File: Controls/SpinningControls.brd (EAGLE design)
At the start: 209.6 x 107.9 mm, 120 parts, among them IC1 S-19246E33H-V5T2U, IC2 SN74LVC1G34DBVR, IC3 SN74LVC1G34DBVR, IC4 SN74LVC1G34DBVR, IC5 TXS0104EDR, J10 SULLINS_PPPC062LFBN-RCSULLINS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, J11 SULLINS_PPPC062LFBN-RCSULLINS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, J12 SULLINS_PPPC062LFBN-RCSULLINS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, J13 SULLINS_PPPC062LFBN-RCSULLINS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, J14 SULLINS_PPPC062LFBN-RCSULLINS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

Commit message: dan tings, 50ohm FPGA inline, 3v3 to 5 logic for SR
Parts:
- R20: device rcl:R0603 -> rcl:R0402
- R5: value (none) -> 10k; device rcl:R0402 -> rcl:R0603
- moved R56 206.3 mm to (113.5, 45.2)
- moved R55 204.4 mm to (112.3, 47.6), turned to 45 degrees
- moved R54 199.1 mm to (108.3, 47.6), turned to 45 degrees
- moved R53 193.6 mm to (104.2, 47.6), turned to 90 degrees
- moved R52 188.7 mm to (101.1, 47.6), turned to 90 degrees
- moved R51 183.8 mm to (98.0, 47.6), turned to 90 degrees
- moved R50 178.9 mm to (94.9, 47.6), turned to 90 degrees
- moved R49 173.5 mm to (90.8, 47.6), turned to 90 degrees
- moved R48 168.6 mm to (87.8, 47.6), turned to 90 degrees
- moved R47 163.9 mm to (84.9, 47.6), turned to 90 degrees
- moved R46 159.1 mm to (82.0, 47.6), turned to 90 degrees
- moved R45 154.0 mm to (78.5, 47.6), turned to 135 degrees
- moved R38 153.2 mm to (113.5, 42.7)
- moved R44 147.8 mm to (73.0, 47.5), turned to 180 degrees
- moved R35 145.8 mm to (102.6, 47.6), turned to 270 degrees
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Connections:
- net 3V3_LOGIC: now also R5.2; no longer R20.2
- net ENC_POS: now also FPGA.43; no longer FPGA.41
- net ENC_POS0: now also FPGA.41; no longer FPGA.43
- net GND: now also R5.1; no longer R20.1
- net N$10: now also FPGA.9; no longer FPGA.4
- net N$11: now also FPGA.7; no longer FPGA.6
- net N$12: now also FPGA.6; no longer FPGA.8
- net N$13: now also FPGA.2; no longer FPGA.10
- net N$15: now also R7.2; no longer R6.2
- net N$16: now also R8.2; no longer R7.2
- net N$18: now also R9.2; no longer R8.2
- net N$19: now also R10.2; no longer R9.2
- net N$2: now also R6.2; no longer R5.2
- net N$20: now also R11.2; no longer R10.2
- net N$21: now also R12.2; no longer R11.2
- net N$22: now also R13.2; no longer R12.2
- net N$23: now also R14.2; no longer R13.2
- net N$24: now also R15.2; no longer R14.2
- net N$25: now also R16.2; no longer R15.2
- net N$27: now also R17.2; no longer R16.2
- net N$28: now also R18.2; no longer R17.2
- net N$29: now also R19.2; no longer R18.2
- net N$30: now also R20.2; no longer R19.2
- net N$34: now also FPGA.26; no longer FPGA.25
- net N$35: now also FPGA.28; no longer FPGA.27
- net N$47: now also FPGA.25; no longer FPGA.26
- net N$48: now also FPGA.27; no longer FPGA.28
- net N$54: now also FPGA.10; no longer FPGA.2
- net N$7: now also FPGA.8; no longer FPGA.5
- net N$8: now also FPGA.5; no longer FPGA.7
- net N$9: now also FPGA.4; no longer FPGA.9
- net SIN12_J4: now also R12.1; no longer R11.1
- net SIN12_J5: now also R16.1; no longer R15.1
- net SIN12_J6: now also R20.1; no longer R19.1
- net SIN34_J3: now also R8.1; no longer R7.1
- net SIN34_J4: now also R11.1; no longer R10.1
- net SIN34_J5: now also R15.1; no longer R14.1
- net SIN34_J6: now also R19.1; no longer R18.1
- net SIN56_J3: now also R7.1; no longer R6.1
- net SIN56_J4: now also R10.1; no longer R9.1
- net SIN56_J5: now also R14.1; no longer R13.1
- net SIN56_J6: now also R18.1; no longer R17.1
- net SIN78_J3: now also R6.1; no longer R5.1
- net SIN78_J4: now also R9.1; no longer R8.1
- net SIN78_J5: now also R13.1; no longer R12.1
- net SIN78_J6: now also R17.1; no longer R16.1
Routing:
- net SIN12_J14: track 15.5 -> 96.0 mm
- net LAT: track 332.4 -> 389.7 mm
- net GSCLK: track 348.3 -> 402.8 mm
- net SCLK: track 317.5 -> 367.4 mm
- net SIN56_J13: track 60.8 -> 13.9 mm
- net SIN78_J13: track 51.0 -> 9.38 mm
- net SIN34_J13: track 52.3 -> 11.4 mm
- net GSCLK_FPGA: track 35.8 -> 76.4 mm
- net SIN12_J6: track 68.8 -> 107.1 mm
- net SIN34_J6: track 67.4 -> 103.4 mm
- net SIN56_J6: track 72.3 -> 105.9 mm
- net SIN78_J6: track 71.0 -> 102.3 mm
- net SIN12_J5: track 74.6 -> 103.6 mm
- net SIN34_J5: track 73.1 -> 99.8 mm
- net SIN56_J5: track 77.7 -> 102.0 mm
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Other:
- board text added: "R6-R56 (50Ω)"

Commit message: to-kyle documentation updates
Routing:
- net ENC_POS: track 285.3 -> 207.8 mm
- net PI_RX: track 91.2 -> 75.6 mm
- net PI_TX: track 94.3 -> 79.1 mm
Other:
- board text added: "NOT ROUTED YET logic level shifter (3v3 to 5)"
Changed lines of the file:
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@@
 v1</text>
 <text x="60.96" y="46.99" size="0.889" layer="21">R6-R56 (50Ω)</text>
+<wire x1="152.4" y1="95.25" x2="152.4" y2="91.44" width="0.1524" layer="21"/>
+<wire x1="152.4" y1="91.44" x2="149.86" y2="91.44" width="0.1524" layer="21"/>
+<wire x1="149.86" y1="91.44" x2="149.86" y2="82.55" width="0.1524" layer="21"/>
+<wire x1="149.86" y1="82.55" x2="166.37" y2="82.55" width="0.1524" layer="21"/>
+<wire x1="166.37" y1="82.55" x2="166.37" y2="86.36" width="0.1524" layer="21"/>
+<wire x1="166.37" y1="86.36" x2="162.56" y2="86.36" width="0.1524" layer="21"/>
+<wire x1="162.56" y1="86.36" x2="162.56" y2="95.25" width="0.1524" layer="21"/>
+<wire x1="162.56" y1="95.25" x2="152.4" y2="95.25" width="0.1524" layer="21"/>
+<text x="163.195" y="86.995" size="0.762" layer="21">NOT ROUTED YET
+logic level shifter (3v3 to 5)</text>
 </plain>
 <attributes>
@@
 <wire x1="115.57" y1="95.25" x2="99.4918" y2="95.25" width="0.1524" layer="16"/>
 <wire x1="170.53" y1="69.85" x2="125.73" y2="69.85" width="0.1524" layer="1"/>
-<wire x1="123.19" y1="72.39" x2="123.19" y2="87.63" width="0.1524" layer="1"/>
 <wire x1="123.19" y1="87.63" x2="115.57" y2="95.25" width="0.1524" layer="1"/>
 <contactref element="IC5" pad="3"/>
-<wire x1="115.57" y1="95.25" x2="160.192" y2="86.36" width="0" layer="19" extent="1-1"/>
+<wire x1="173.24" y1="72.56" x2="160.192" y2="86.36" width="0" layer="19" extent="1-1"/>
+<wire x1="123.19" y1="87.63" x2="123.19" y2="72.39" width="0" layer="19" extent="1-1"/>
 </signal>
 <signal name="PI_RX">
@@
 <via x="115.57" y="96.52" extent="1-16" drill="0.35"/>
 <wire x1="168.498" y1="70.358" x2="126.111" y2="70.358" width="0.1524" layer="1"/>
-<wire x1="123.698" y1="72.771" x2="123.698" y2="88.392" width="0.1524" layer="1"/>
 <wire x1="113.411" y1="95.631" x2="114.3" y2="96.52" width="0.1524" layer="16"/>
 <wire x1="114.3" y1="96.52" x2="115.57" y2="96.52" width="0.1524" layer="16"/>
@@
 <wire x1="102.489" y1="95.631" x2="113.411" y2="95.631" width="0.1524" layer="16"/>
 <contactref element="IC5" pad="4"/>
-<wire x1="115.57" y1="96.52" x2="160.192" y2="87.63" width="0" layer="19" extent="1-1"/>
+<wire x1="170.7" y1="72.56" x2="160.192" y2="87.63" width="0" layer="19" extent="1-1"/>
+<wire x1="123.698" y1="88.392" x2="123.698" y2="72.771" width="0" layer="19" extent="1-1"/>
 </signal>
 <signal name="LAT">
@@
 <wire x1="203.2" y1="83.3628" x2="201.3712" y2="81.534" width="0.1524" layer="1"/>
 <wire x1="106.0958" y1="99.06" x2="114.3" y2="99.06" width="0.1524" layer="16"/>
-<wire x1="124.46" y1="88.9" x2="201.93" y2="88.9" width="0.1524" layer="1"/>
 <wire x1="205.232" y1="79.4512" x2="203.1492" y2="81.534" width="0.1524" layer="1"/>
 <wire x1="201.3712" y1="81.534" x2="203.1492" y2="81.534" width="0.1524" layer="1"/>
@@
 <wire x1="201.3712" y1="81.534" x2="197.7272" y2="77.89" width="0.1524" layer="1"/>
 <wire x1="197.7272" y1="77.89" x2="194.31" y2="77.89" width="0.1524" layer="1"/>
+<wire x1="124.46" y1="88.9" x2="160.192" y2="88.9" width="0" layer="19" extent="1-1"/>
 <wire x1="194.31" y1="77.89" x2="160.192" y2="88.9" width="0" layer="19" extent="1-1"/>
 </signal>

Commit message: full routing layout and schematic
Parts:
- moved R22 7.00 mm to (100.8, 4.45), turned to 45 degrees
- moved R32 1.55 mm to (94.9, 47.6)
- moved R33 1.55 mm to (98.0, 47.6)
- moved R50 1.55 mm to (93.3, 47.6)
- moved R51 1.55 mm to (96.4, 47.6)
- moved C36 1.02 mm to (152.1, 87.6), turned to 180 degrees
- moved C35 0.81 mm to (152.1, 83.8), turned to 180 degrees
- moved C34 0.81 mm to (162.8, 83.8), turned to 0 degrees
- moved R45 0.25 mm to (78.2, 47.6)
- turned R38 to 180 degrees
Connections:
- net N$34: now also FPGA.25; no longer FPGA.26
- net N$35: now also FPGA.27; no longer FPGA.28
- net N$39: now also FPGA.38; no longer FPGA.37
- net N$47: now also FPGA.26; no longer FPGA.25
- net N$48: now also FPGA.28; no longer FPGA.27
- net N$52: now also FPGA.37; no longer FPGA.38
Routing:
- net PI_TX_SR: track 0.00 -> 67.2 mm, vias 0 -> 1
- net PI_RX_SR: track 0.00 -> 58.2 mm, vias 0 -> 1
- net 3V3_LOGIC: track 506.9 -> 564.4 mm
- net ENC_POS_SR: track 0.00 -> 56.3 mm, vias 0 -> 1
- net PI_TX: track 79.1 -> 28.2 mm
- net PI_RX: track 75.6 -> 26.3 mm
- net SIN34_J13: track 11.4 -> 47.2 mm
- net GND: track 60.8 -> 95.5 mm, vias 59 -> 68
- net SIN56_J13: track 13.9 -> 48.2 mm
- net SIN78_J13: track 9.38 -> 43.2 mm
- net SIN12_J13: track 38.2 -> 58.6 mm
- net SIN56_J14: track 59.3 -> 79.5 mm
- net SIN78_J14: track 51.7 -> 71.3 mm
- net ENC_POS: track 207.8 -> 226.4 mm, vias 1 -> 0
- net SIN34_J14: track 65.2 -> 81.7 mm
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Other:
- board text added: "R22-R56 (50Ω)"
- board text added: "R6-R21 (50Ω)"
- board text removed: "NOT ROUTED YET logic level shifter (3v3 to 5)"
- board text removed: "R6-R56 (50Ω)"

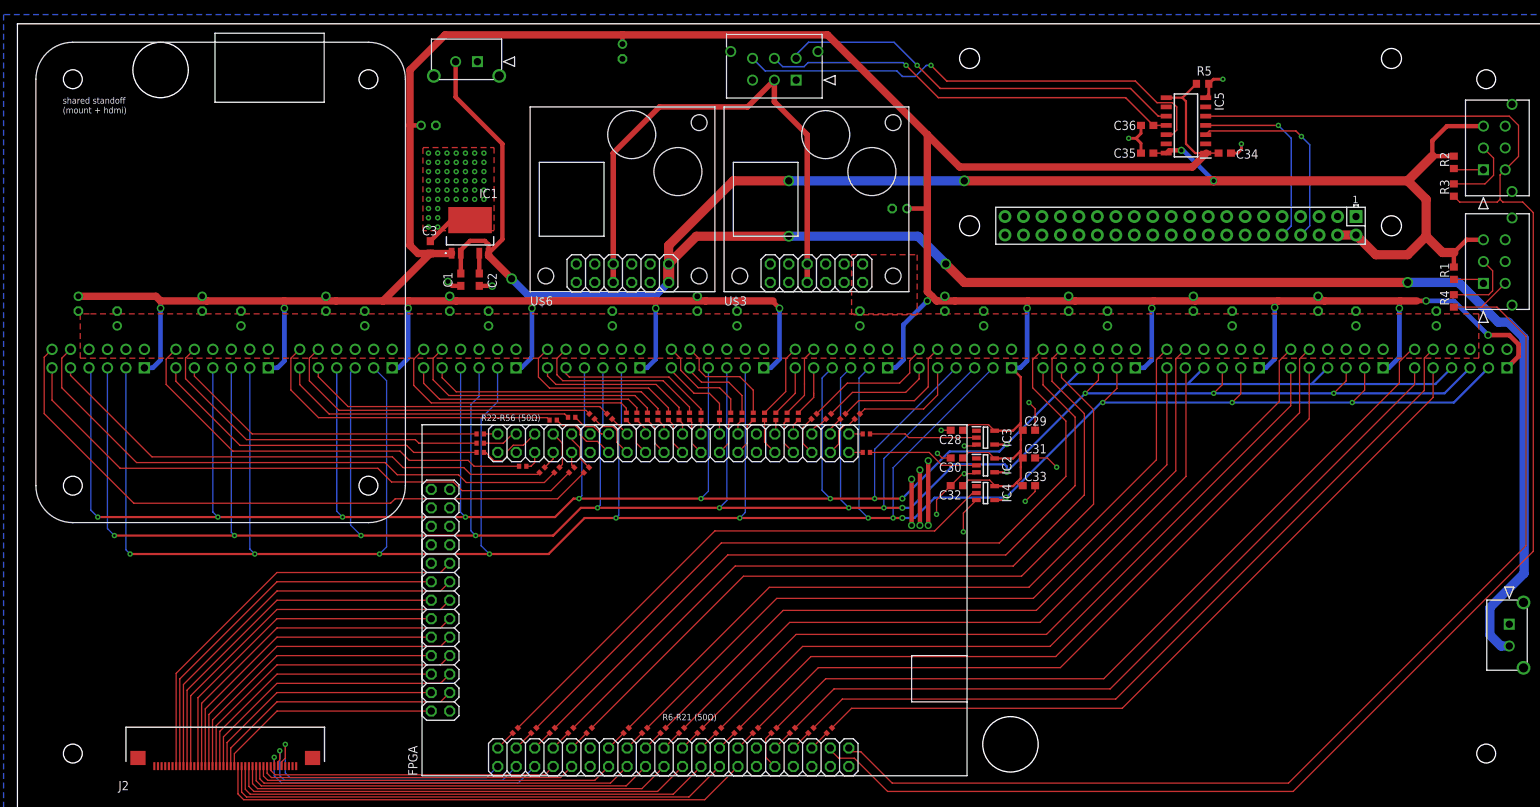
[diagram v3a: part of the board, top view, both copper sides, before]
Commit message: added mounting holes; processed CAM and schem PDF
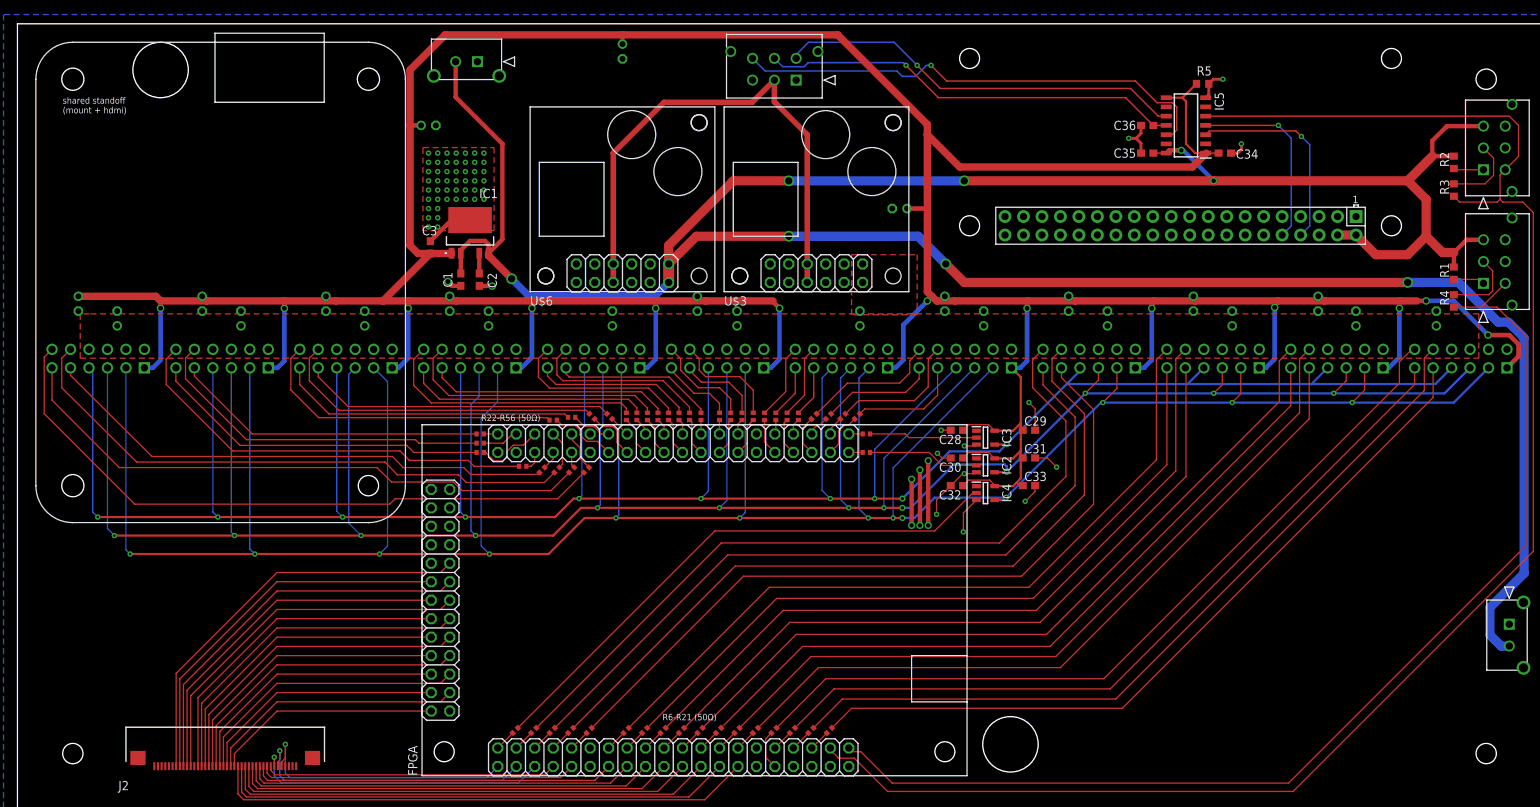
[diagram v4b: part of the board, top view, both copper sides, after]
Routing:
- net 3V3_LOGIC: track 564.4 -> 565.2 mm
